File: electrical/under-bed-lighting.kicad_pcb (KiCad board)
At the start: 2 copper layers, 75 parts, among them J1 PJ-002AH, J10 0705430002, J11 0705430002, J2 0705430002, J3 0705430001, J4 0705430001, J5 0705430001, J6 0705430002, J7 0705430002, J8 0705430002, J9 0705430002, Q1 AO3401A, Q2 AO3400A, Q3 AO3400A, Q4 AO3400A, U1 ESP32-C3 Super Mini, U2 LMR51606YFDBVR, U3 SN74LVC08ADR

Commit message: working on layout
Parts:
- moved R19 135.0 mm to (97.2, 78.8), turned to 90 degrees
- moved F9 131.9 mm to (99.7, 78.8), turned to 90 degrees
- moved R17 131.2 mm to (109.2, 88.9), turned to 90 degrees
- moved F8 128.3 mm to (111.8, 88.9), turned to 90 degrees
- moved R21 101.2 mm to (108.6, 78.7), turned to 90 degrees
- moved R15 98.0 mm to (97.8, 88.9), turned to 90 degrees
- moved F10 97.9 mm to (111.1, 78.8), turned to 90 degrees
- moved F7 94.9 mm to (100.3, 88.9), turned to 90 degrees
- moved R13 74.1 mm to (109.2, 99.1), turned to 90 degrees
- moved F6 71.0 mm to (111.8, 99.1), turned to -90 degrees
- moved J11 55.5 mm to (108.6, 83.2)
- moved J10 55.5 mm to (97.2, 83.2)
- moved U3 39.9 mm to (113.7, 45.1)
- moved J8 30.6 mm to (97.8, 93.3)
- moved J9 29.4 mm to (109.2, 93.3)
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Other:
- board outline added: 138.4 x 41.3 mm

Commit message: Continue layout...
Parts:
- J3, J4, J5: footprint Connector_PinHeader_2.54mm:PinHeader_1x02_P2.54mm_Vertical -> !Connectors:molex_0705430001
- moved R7 181.4 mm to (52.7, 102.2)
- moved R5 175.0 mm to (56.5, 97.8), turned to 180 degrees
- moved R9 170.9 mm to (68.6, 105.4)
- moved C10 155.9 mm to (38.7, 81.9), turned to -90 degrees
- moved D8 154.3 mm to (35.6, 81.9)
- moved C7 148.1 mm to (68.6, 95.2)
- moved C9 146.5 mm to (38.7, 77.5), turned to 90 degrees
- moved D7 144.8 mm to (35.6, 77.5)
- moved R10 113.8 mm to (120.7, 82.5), turned to -90 degrees
- moved F4 106.7 mm to (123.8, 78.1), turned to 180 degrees
- moved F3 106.0 mm to (123.8, 90.8), turned to 180 degrees
- moved F2 105.5 mm to (123.8, 103.5), turned to 180 degrees
- moved Q4 105.2 mm to (124.5, 82.5)
- moved R8 103.2 mm to (128.9, 85.7), turned to -90 degrees
- moved R6 102.7 mm to (128.9, 98.4), turned to -90 degrees
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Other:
- board size 138.4 x 41.3 mm -> 114.3 x 41.3 mm

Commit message: Layout complete
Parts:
- added H1: MountingHole_Pad, MountingHole:MountingHole_2mm, F.Cu at (36.0, 70.0)
- added H2: MountingHole_Pad, MountingHole:MountingHole_2mm, F.Cu at (36.0, 120.0)
- added H3: MountingHole_Pad, MountingHole:MountingHole_2mm, F.Cu at (126.0, 70.0)
- added H4: MountingHole_Pad, MountingHole:MountingHole_2mm, F.Cu at (126.0, 120.0)
- L1: value 74404064180 -> SWPA6045S180MT
- moved C1 190.4 mm to (35.6, 87.1), turned to -90 degrees
- moved C2 186.1 mm to (38.7, 87.1), turned to -90 degrees
- moved D11 171.0 mm to (64.8, 76.8), turned to 180 degrees
- moved C13 169.7 mm to (61.6, 77.5), turned to -90 degrees
- moved D9 169.6 mm to (65.4, 91.4), turned to 180 degrees
- moved C11 169.6 mm to (61.0, 90.2), turned to 90 degrees
- moved D10 158.0 mm to (65.4, 85.7), turned to 180 degrees
- moved C12 157.7 mm to (61.0, 86.4), turned to -90 degrees
- moved R16 156.5 mm to (76.2, 81.9), turned to 90 degrees
- moved R20 147.8 mm to (76.2, 69.8), turned to 90 degrees
- moved R22 140.9 mm to (92.1, 69.8), turned to 90 degrees
- moved R14 140.1 mm to (92.1, 81.9), turned to 90 degrees
- moved R12 129.7 mm to (108.0, 69.8), turned to 90 degrees
- moved R18 122.8 mm to (108.0, 81.9), turned to 90 degrees
- moved F5 31.6 mm to (112.4, 69.8)
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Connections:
- U1 pad 3: unconnected-(U1-GPIO7-Pad3) -> /LED2
- U1 pad 4: /LED2 -> unconnected-(U1-GPIO8-Pad4)
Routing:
- net /PIR1: track 0.00 -> 132.5 mm, vias 0 -> 3
- net /PIR2: track 0.00 -> 89.1 mm, vias 0 -> 2
- net /LEDEN: track 0.00 -> 75.6 mm, vias 0 -> 1
- net Net-(Q2-G): track 0.00 -> 75.3 mm, vias 0 -> 2
- net /PIR3: track 0.00 -> 67.1 mm, vias 0 -> 4
- net Net-(Q3-G): track 0.00 -> 65.3 mm, vias 0 -> 2
- net /PIR4: track 0.00 -> 63.0 mm
- net GND: track 0.00 -> 58.5 mm, vias 0 -> 32
- net /LED1: track 0.00 -> 54.6 mm, vias 0 -> 1
- net Net-(Q4-G): track 0.00 -> 45.3 mm, vias 0 -> 2
- net /PIR6: track 0.00 -> 42.2 mm
- net /LED3: track 0.00 -> 32.9 mm, vias 0 -> 1
- net +3.3V: track 0.00 -> 31.9 mm, vias 0 -> 14
- net /PIR5: track 0.00 -> 29.8 mm
- net /LED2: track 0.00 -> 27.9 mm, vias 0 -> 1
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- added copper zone on In2.Cu, net +24V
- added copper zone on In2.Cu, net +3.3V
- added copper zone on In1.Cu, net GND
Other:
- board size 114.3 x 41.3 mm -> 100 x 60 mm
- copper layers 2 -> 4
- board text added: "${TITLE}"
- board text added: "${TITLE} REV ${REVISION}"

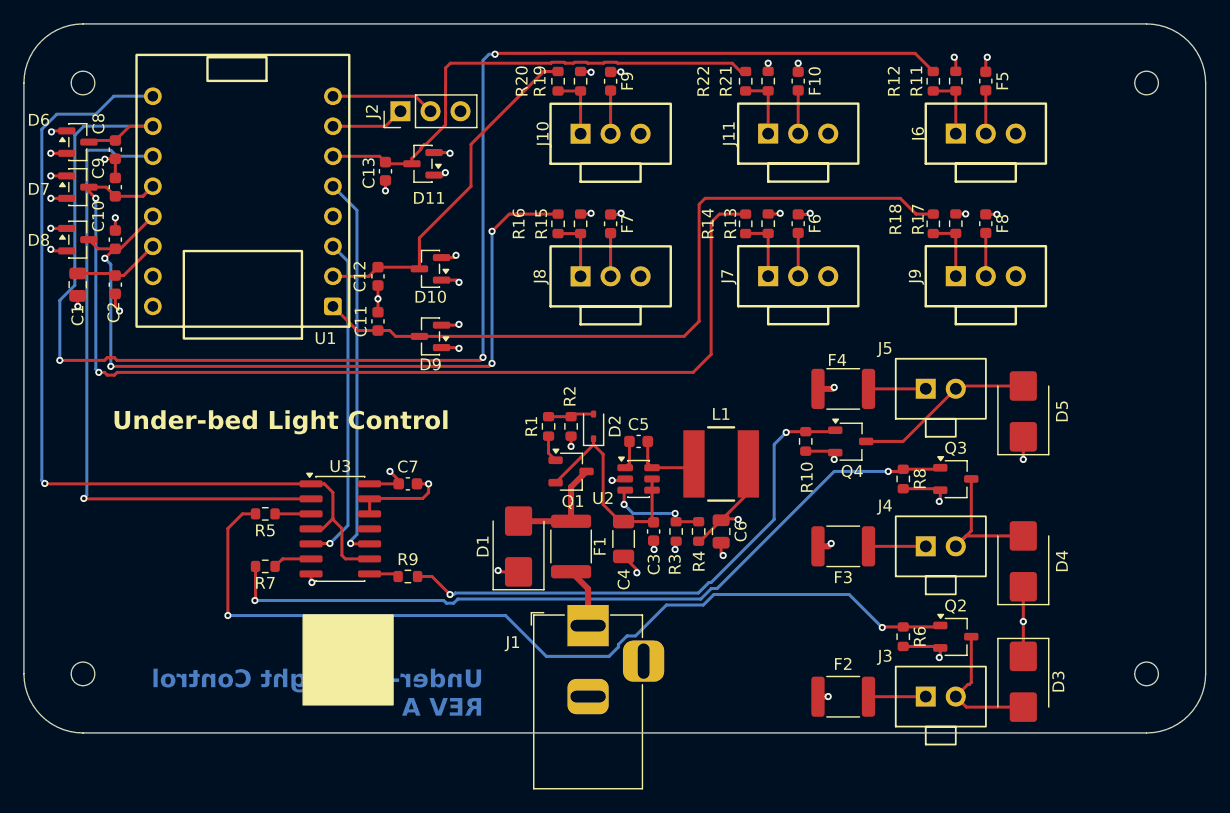
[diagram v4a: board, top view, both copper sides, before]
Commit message: Finished and submitted to JLCPCB
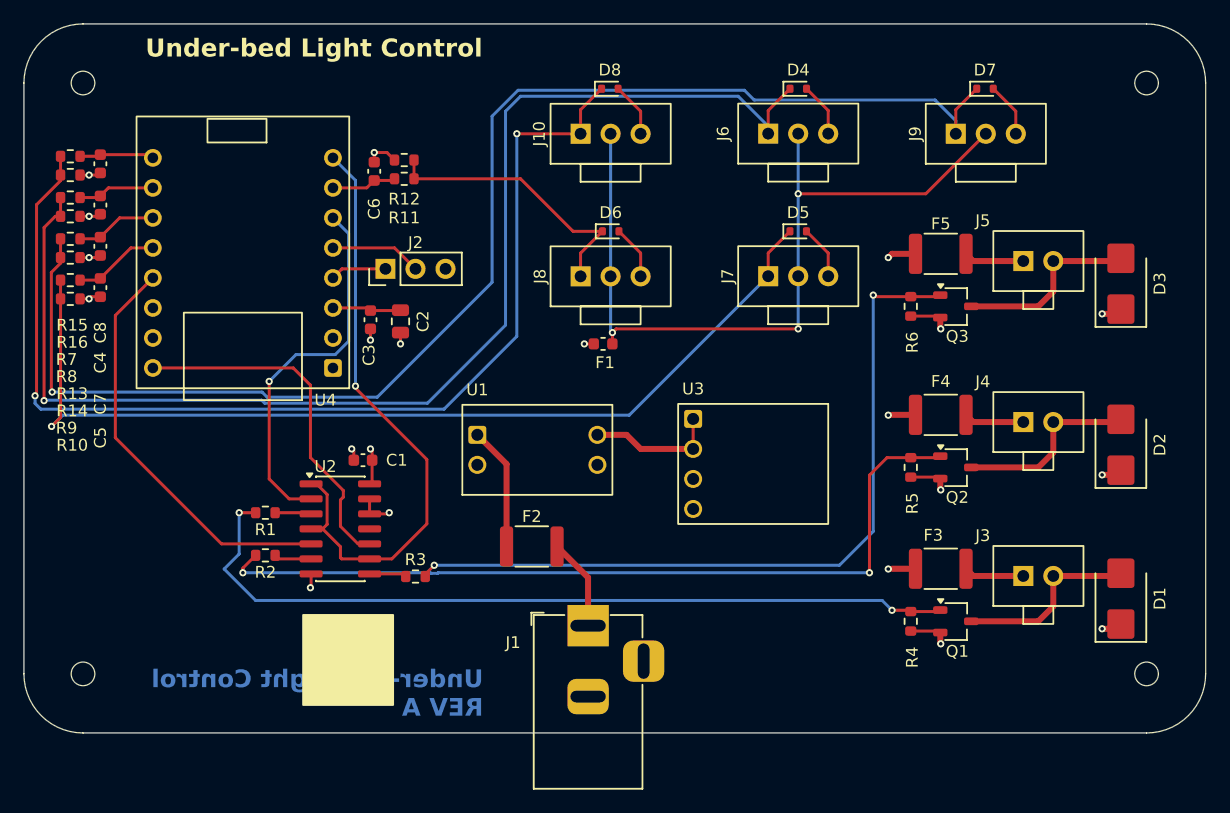
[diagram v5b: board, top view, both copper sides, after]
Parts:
- removed C13: 47nF, Capacitor_SMD:C_0603_1608Metric
- removed the C3 at (84.3, 108.0)
- removed the C4 at (81.7, 108.6)
- removed the C5 at (83.0, 100.3)
- removed the C6 at (90.0, 108.0)
- removed the D1 at (72.9, 109.2)
- removed D10, D11, D9: BAT54SLT1G, Package_TO_SOT_SMD:SOT-23
- removed the D2 at (79.2, 99.1)
- removed F10, F6, F7, F8, F9: 0603L010YR, Fuse:Fuse_0603_1608Metric
- removed the F5 at (112.4, 69.8)
- removed J11: 0705430002, !Connectors:molex_705430002
- removed L1: SWPA6045S180MT, !Inductors:WE-LQS_6045
- removed the Q1 at (77.3, 102.9)
- removed R21: 100kΩ, Resistor_SMD:R_0603_1608Metric
- removed R22: 47kΩ, Resistor_SMD:R_0603_1608Metric
- removed the R4 at (86.2, 108.0)
- removed the R5 at (51.4, 106.5)
- removed the R7 at (51.4, 110.9)
- removed the R9 at (63.5, 111.8)
- removed the U2 at (83.0, 103.5)
- added D4: ESD5Z3.3TG5, Diode_SMD:D_SOD-523, F.Cu at (96.5, 70.5)
- added D5: ESD5Z3.3TG5, Diode_SMD:D_SOD-523, F.Cu at (96.5, 82.5)
- added F1: 0603L010YR, Fuse:Fuse_0603_1608Metric, F.Cu at (80.0, 92.1)
- added U1: RVP_5358, !Pololu:RVP_5358, F.Cu at (69.4, 99.8)
- added U3: D36V6F3, !Pololu:D36V6x, F.Cu at (87.6, 98.4)
- C4: renamed from C8; value 47nF -> 100nF
- C5: renamed from C9; value 47nF -> 100nF
- C6: renamed from C10; value 47nF -> 100nF
- C7: renamed from C11; value 47nF -> 100nF
- C8: renamed from C12; value 47nF -> 100nF
- D6, D7, D8: value BAT54SLT1G -> ESD5Z3.3TG5; footprint Package_TO_SOT_SMD:SOT-23 -> Diode_SMD:D_SOD-523
- R11: renamed from R16; value 47kΩ -> 10kΩ
- R13: renamed from R18; value 47kΩ -> 10kΩ
- R15: renamed from R20; value 47kΩ -> 10kΩ
- R2: value 10kΩ -> 100Ω
- R3: value 100kΩ -> 100Ω
- R7: renamed from R12; value 47kΩ -> 10kΩ
- R9: renamed from R14; value 47kΩ -> 10kΩ
- U4: renamed from U1; value ESP32-C3 Super Mini -> ESP32-C3 OLED
- moved D7 77.2 mm to (112.3, 70.5)
- moved R8 75.8 mm to (34.9, 81.3), turned to 0 degrees
- moved R14 75.0 mm to (34.9, 84.8), turned to 0 degrees
- moved R7 73.7 mm to (34.9, 79.7), turned to 0 degrees
- moved R13 73.0 mm to (34.9, 83.2), turned to 0 degrees
- moved R10 59.4 mm to (34.9, 88.3), turned to 0 degrees
- moved R9 57.3 mm to (34.9, 86.7), turned to 0 degrees
- moved D8 46.8 mm to (80.6, 70.5)
- moved D6 45.7 mm to (80.7, 82.5)
- moved R16 43.9 mm to (34.9, 77.8), turned to 0 degrees
- moved R15 41.8 mm to (34.9, 76.2), turned to 0 degrees
- moved R2 28.1 mm to (51.4, 110.0), turned to 180 degrees
- moved C2 27.5 mm to (62.9, 90.2)
- moved C8 25.4 mm to (37.5, 76.8)
- moved R1 25.0 mm to (51.4, 106.4), turned to 180 degrees
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- renumbered C7 to C1, C1 to C2, C2 to C3, D3 to D1, D4 to D2, D5 to D3, F1 to F2, F2 to F3, F3 to F4, F4 to F5, Q2 to Q1, Q3 to Q2, Q4 to Q3, R13 to R10, R15 to R12, R17 to R14, R19 to R16, R6 to R4, R8 to R5, R10 to R6, R11 to R8, U3 to U2
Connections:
- D6 pad 1: GND -> Net-(D6-K1)
- D6 pad 2: +3.3V -> GND
- D7 pad 1: GND -> Net-(D7-K1)
- D7 pad 2: +3.3V -> GND
- D8 pad 1: GND -> Net-(D8-K1)
- D8 pad 2: +3.3V -> GND
- J10 pad 1: Net-(J10-Pin_1) -> Net-(D8-K1)
- J10 pad 2: Net-(J10-Pin_2) -> /PIR Sensor1/PWR
- J6 pad 2: Net-(J6-Pin_2) -> /PIR Sensor1/PWR
- J7 pad 2: Net-(J7-Pin_2) -> /PIR Sensor1/PWR
- J8 pad 1: Net-(J8-Pin_1) -> Net-(D6-K1)
- J8 pad 2: Net-(J8-Pin_2) -> /PIR Sensor1/PWR
- J9 pad 1: Net-(J9-Pin_1) -> Net-(D7-K1)
- J9 pad 2: Net-(J9-Pin_2) -> /PIR Sensor1/PWR
- Q1 pad 1: Net-(Q2-G) -> /LED Driver1/PWM
- Q2 pad 1: Net-(Q3-G) -> /LED Driver2/PWM
- Q3 pad 1: Net-(Q4-G) -> /LED Driver3/PWM
- R1 pad 1: Net-(Q1-G) -> Net-(R1-Pad1)
- R1 pad 2: Net-(D2-A) -> /LED Driver1/PWM
- R11 pad 1: Net-(J8-Pin_1) -> Net-(D6-K1)
- R12 pad 1: Net-(J8-Pin_1) -> Net-(D6-K1)
- R13 pad 1: Net-(J9-Pin_1) -> Net-(D7-K1)
- R14 pad 1: Net-(J9-Pin_1) -> Net-(D7-K1)
- R15 pad 1: Net-(J10-Pin_1) -> Net-(D8-K1)
- R16 pad 1: Net-(J10-Pin_1) -> Net-(D8-K1)
- R2 pad 1: Net-(D2-A) -> Net-(R2-Pad1)
- R2 pad 2: GND -> /LED Driver2/PWM
- R3 pad 1: +3.3V -> Net-(R3-Pad1)
- R3 pad 2: Net-(U2-FB) -> /LED Driver3/PWM
- R4 pad 1: Net-(Q2-G) -> /LED Driver1/PWM
- R5 pad 1: Net-(Q3-G) -> /LED Driver2/PWM
- R6 pad 1: Net-(Q4-G) -> /LED Driver3/PWM
- U2 pad 1: /LEDEN -> Net-(U4-GPIO0)
- U2 pad 3: Net-(R5-Pad1) -> Net-(R1-Pad1)
- U2 pad 4: /LEDEN -> Net-(U4-GPIO0)
- U2 pad 6: Net-(R7-Pad1) -> Net-(R2-Pad1)
- U2 pad 8: Net-(R9-Pad1) -> Net-(R3-Pad1)
- U2 pad 9: /LEDEN -> Net-(U4-GPIO0)
- U4 pad 1: /PIR4 -> unconnected-(U4-5V-Pad1)
- U4 pad 11: /LED1 -> /PIR4
- U4 pad 13: /PIR3 -> /LED2
- U4 pad 14: +3.3V -> unconnected-(U4-GPIO8-Pad14)
- U4 pad 15: GND -> unconnected-(U4-GPIO9-Pad15)
- U4 pad 16: unconnected-(U1-5V-Pad16) -> /LED3
- U4 pad 2: /PIR5 -> GND
- U4 pad 3: /LED2 -> +3.3V
- U4 pad 4: unconnected-(U1-GPIO8-Pad4) -> /RXD
- U4 pad 5: /LED3 -> /TXD
- U4 pad 6: /PIR6 -> /LED1
- U4 pad 7: /RXD -> /PIR3
- U4 pad 8: /TXD -> Net-(U4-GPIO0)
- U4 pad 9: /LEDEN -> /PIR5
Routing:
- net /PIR1: track 132.5 -> 6.30 mm, vias 3 -> 0
- net Net-(D7-K1): track 0.00 -> 115.7 mm, vias 0 -> 1
- net Net-(D4-K1): track 5.51 -> 106.9 mm, vias 0 -> 1
- net Net-(D8-K1): track 0.00 -> 92.4 mm, vias 0 -> 2
- net /PIR2: track 89.1 -> 7.09 mm, vias 2 -> 0
- net Net-(D5-K1): track 5.51 -> 83.2 mm, vias 0 -> 1
- net /LEDEN: track 75.6 -> 0.00 mm, vias 1 -> 0
- net Net-(Q2-G): track 75.3 -> 0.00 mm, vias 2 -> 0
- net /LED Driver2/PWM: track 0.00 -> 69.7 mm, vias 0 -> 2
- net /LED Driver1/PWM: track 0.00 -> 69.0 mm, vias 0 -> 2
- net /PIR Sensor1/PWR: track 0.00 -> 68.2 mm, vias 0 -> 3
- net Net-(Q3-G): track 65.3 -> 0.00 mm, vias 2 -> 0
- net /LED Driver3/PWM: track 0.00 -> 65.0 mm, vias 0 -> 2
- net /PIR3: track 67.1 -> 5.33 mm, vias 4 -> 0
- net +24V: track 8.68 -> 68.3 mm
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- removed copper zone on In2.Cu, net +24V
